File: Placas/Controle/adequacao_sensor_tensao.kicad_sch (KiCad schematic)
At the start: 6 parts, among them J5 Conn_01x02_Pin, U3 LV25-P

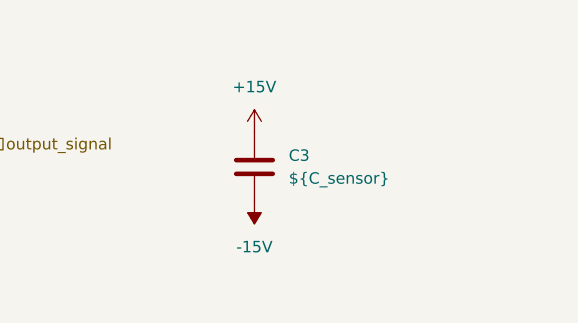
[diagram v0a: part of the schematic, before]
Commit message: Adição de circuitos opcionais para PWM
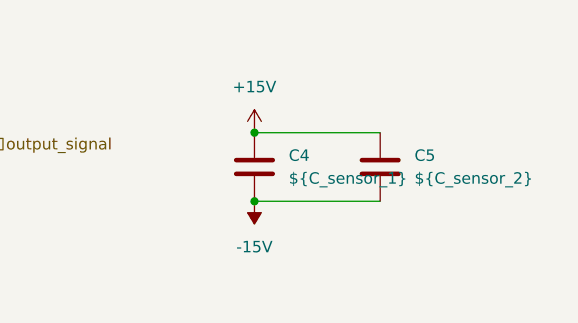
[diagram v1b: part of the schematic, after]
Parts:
- added C5: ${C_sensor_2}, Capacitor_THT:C_Disc_D8.0mm_W5.0mm_P7.50mm, symbol Device:C
- C4: renamed from C3; value ${C_sensor} -> ${C_sensor_1}
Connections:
- net +15V: now also C5.1
- net -15V: now also C5.2
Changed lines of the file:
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@@
+		(color 0 0 0 0)
+	)
+	(junction
+		(at 161.29 71.12)
+		(diameter 0)
+		(color 0 0 0 0)
+	)
+	(junction
+		(at 161.29 78.74)
+		(diameter 0)
 		(color 0 0 0 0)
 	)
@@
 	(wire
 		(pts
-			(xy 60.96 72.39) (xy 60.96 74.93)
+			(xy 161.29 78.74) (xy 175.26 78.74)
 		)
 		(stroke
@@
 	(wire
 		(pts
-			(xy 120.65 72.39) (xy 109.22 72.39)
+			(xy 60.96 72.39) (xy 60.96 74.93)
 		)
 		(stroke
@@
 	(wire
 		(pts
-			(xy 120.65 72.39) (xy 132.08 72.39)
+			(xy 120.65 72.39) (xy 109.22 72.39)
 		)
 		(stroke
@@
 	(wire
 		(pts
-			(xy 85.09 69.85) (xy 88.9 69.85)
+			(xy 120.65 72.39) (xy 132.08 72.39)
 		)
 		(stroke
@@
 	(wire
 		(pts
+			(xy 85.09 69.85) (xy 88.9 69.85)
+		)
+		(stroke
+			(width 0)
+			(type default)
+		)
+	)
+	(wire
+		(pts
 			(xy 74.93 69.85) (xy 77.47 69.85)
+		)
+		(stroke
+			(width 0)
+			(type default)
+		)
+	)
+	(wire
+		(pts
+			(xy 161.29 71.12) (xy 175.26 71.12)
 		)
 		(stroke
@@
 		(dnp no)
 		(fields_autoplaced yes)
-		(property "Reference" "#PWR18"
+		(property "Reference" "#PWR20"
 			(at 161.29 74.93 0)
 			(effects
@@
 			(project "board"
 				(path "/01568b53-f202-4f02-9c1a-9c10c7610b4b/64ed1ee1-6201-4cd1-840c-b46b599d55ab/9701d4b2-9f70-4dc2-8f65-3cb2cc418c7b"
-					(reference "#PWR18")
-					(unit 1)
-				)
-				(path "/01568b53-f202-4f02-9c1a-9c10c7610b4b/64ed1ee1-6201-4cd1-840c-b46b599d55ab/d6523acf-4a35-49b3-8df2-392463f7dfc0"
-					(reference "#PWR13")
+					(reference "#PWR20")
+					(unit 1)
+				)
+				(path "/01568b53-f202-4f02-9c1a-9c10c7610b4b/64ed1ee1-6201-4cd1-840c-b46b599d55ab/d6523acf-4a35-49b3-8df2-392463f7dfc0"
+					(reference "#PWR15")
 					(unit 1)
 				)
@@
 	)
 	(symbol
+		(lib_id "Device:C")
+		(at 175.26 74.93 0)
+		(unit 1)
+		(exclude_from_sim no)
+		(in_bom yes)
+		(on_board yes)
+		(dnp no)
+		(fields_autoplaced yes)
+		(property "Reference" "C5"
+			(at 179.07 73.6599 0)
+			(effects
+				(font
+					(size 1.27 1.27)
+				)
+				(justify left)
+			)
+		)
+		(property "Value" "${C_sensor_2}"
+			(at 179.07 76.1999 0)
+			(effects
+				(font
+					(size 1.27 1.27)
+				)
+				(justify left)
+			)
+		)
+		(property "Footprint" "Capacitor_THT:C_Disc_D8.0mm_W5.0mm_P7.50mm"
+			(at 176.2252 78.74 0)
+			(effects
+				(font
+					(size 1.27 1.27)
+				)
+				(hide yes)
+			)
+		)
+		(property "Datasheet" "~"
+			(at 175.26 74.93 0)
+			(effects
+				(font
+					(size 1.27 1.27)
+				)
+				(hide yes)
+			)
+		)
+		(property "Description" "Unpolarized capacitor"
+			(at 175.26 74.93 0)
+			(effects
+				(font
+					(size 1.27 1.27)
+				)
+				(hide yes)
+			)
+		)
+		(pin "1"
+		)
+		(pin "2"
+		)
+		(instances
+			(project "Controle"
+				(path "/01568b53-f202-4f02-9c1a-9c10c7610b4b/64ed1ee1-6201-4cd1-840c-b46b599d55ab/9701d4b2-9f70-4dc2-8f65-3cb2cc418c7b"
+					(reference "C5")
+					(unit 1)
+				)
+				(path "/01568b53-f202-4f02-9c1a-9c10c7610b4b/64ed1ee1-6201-4cd1-840c-b46b599d55ab/d6523acf-4a35-49b3-8df2-392463f7dfc0"
+					(reference "C3")
+					(unit 1)
+				)
+			)
+		)
+	)
+	(symbol
 		(lib_id "Sensor_Voltage:LV25-P")
 		(at 99.06 72.39 0)
@@
 		(dnp no)
 		(fields_autoplaced yes)
-		(property "Reference" "#PWR15"
+		(property "Reference" "#PWR17"
 			(at 99.06 68.58 0)
 			(effects
@@
 			(project "board"
 				(path "/01568b53-f202-4f02-9c1a-9c10c7610b4b/64ed1ee1-6201-4cd1-840c-b46b599d55ab/9701d4b2-9f70-4dc2-8f65-3cb2cc418c7b"
-					(reference "#PWR15")
-					(unit 1)
-				)
-				(path "/01568b53-f202-4f02-9c1a-9c10c7610b4b/64ed1ee1-6201-4cd1-840c-b46b599d55ab/d6523acf-4a35-49b3-8df2-392463f7dfc0"
-					(reference "#PWR10")
+					(reference "#PWR17")
+					(unit 1)
+				)
+				(path "/01568b53-f202-4f02-9c1a-9c10c7610b4b/64ed1ee1-6201-4cd1-840c-b46b599d55ab/d6523acf-4a35-49b3-8df2-392463f7dfc0"
+					(reference "#PWR12")
 					(unit 1)
 				)
@@
 		(dnp no)
 		(fields_autoplaced yes)
-		(property "Reference" "C3"
+		(property "Reference" "C4"
 			(at 165.1 73.6599 0)
 			(effects
@@
 			)
 		)
-		(property "Value" "${C_sensor}"
+		(property "Value" "${C_sensor_1}"
 			(at 165.1 76.1999 0)
 			(effects
@@
 			(project "board"
 				(path "/01568b53-f202-4f02-9c1a-9c10c7610b4b/64ed1ee1-6201-4cd1-840c-b46b599d55ab/9701d4b2-9f70-4dc2-8f65-3cb2cc418c7b"
-					(reference "C3")
+					(reference "C4")
 					(unit 1)
 				)
@@
 		(dnp no)
 		(fields_autoplaced yes)
-		(property "Reference" "#PWR16"
+		(property "Reference" "#PWR18"
 			(at 99.06 76.2 0)
 			(effects
@@
 			(project "board"
 				(path "/01568b53-f202-4f02-9c1a-9c10c7610b4b/64ed1ee1-6201-4cd1-840c-b46b599d55ab/9701d4b2-9f70-4dc2-8f65-3cb2cc418c7b"
-					(reference "#PWR16")
-					(unit 1)
-				)
-				(path "/01568b53-f202-4f02-9c1a-9c10c7610b4b/64ed1ee1-6201-4cd1-840c-b46b599d55ab/d6523acf-4a35-49b3-8df2-392463f7dfc0"
-					(reference "#PWR11")
+					(reference "#PWR18")
+					(unit 1)
+				)
+				(path "/01568b53-f202-4f02-9c1a-9c10c7610b4b/64ed1ee1-6201-4cd1-840c-b46b599d55ab/d6523acf-4a35-49b3-8df2-392463f7dfc0"
+					(reference "#PWR13")
 					(unit 1)
 				)
@@
 		(dnp no)
 		(fields_autoplaced yes)
-		(property "Reference" "#PWR17"
+		(property "Reference" "#PWR19"
 			(at 120.65 90.17 0)
 			(effects
@@
 			(project "board"
 				(path "/01568b53-f202-4f02-9c1a-9c10c7610b4b/64ed1ee1-6201-4cd1-840c-b46b599d55ab/9701d4b2-9f70-4dc2-8f65-3cb2cc418c7b"
-					(reference "#PWR17")
-					(unit 1)
-				)
-				(path "/01568b53-f202-4f02-9c1a-9c10c7610b4b/64ed1ee1-6201-4cd1-840c-b46b599d55ab/d6523acf-4a35-49b3-8df2-392463f7dfc0"
-					(reference "#PWR12")
+					(reference "#PWR19")
+					(unit 1)
+				)
+				(path "/01568b53-f202-4f02-9c1a-9c10c7610b4b/64ed1ee1-6201-4cd1-840c-b46b599d55ab/d6523acf-4a35-49b3-8df2-392463f7dfc0"
+					(reference "#PWR14")
 					(unit 1)
 				)
@@
 		(dnp no)
 		(fields_autoplaced yes)
-		(property "Reference" "#PWR19"
+		(property "Reference" "#PWR21"
 			(at 161.29 74.93 0)
 			(effects
@@
 			(project "board"
 				(path "/01568b53-f202-4f02-9c1a-9c10c7610b4b/64ed1ee1-6201-4cd1-840c-b46b599d55ab/9701d4b2-9f70-4dc2-8f65-3cb2cc418c7b"
-					(reference "#PWR19")
-					(unit 1)
-				)
-				(path "/01568b53-f202-4f02-9c1a-9c10c7610b4b/64ed1ee1-6201-4cd1-840c-b46b599d55ab/d6523acf-4a35-49b3-8df2-392463f7dfc0"
-					(reference "#PWR14")
-					(unit 1)
-				)
+					(reference "#PWR21")
+					(unit 1)
+				)
+				(path "/01568b53-f202-4f02-9c1a-9c10c7610b4b/64ed1ee1-6201-4cd1-840c-b46b599d55ab/d6523acf-4a35-49b3-8df2-392463f7dfc0"
+					(reference "#PWR16")
+					(unit 1)
+				)

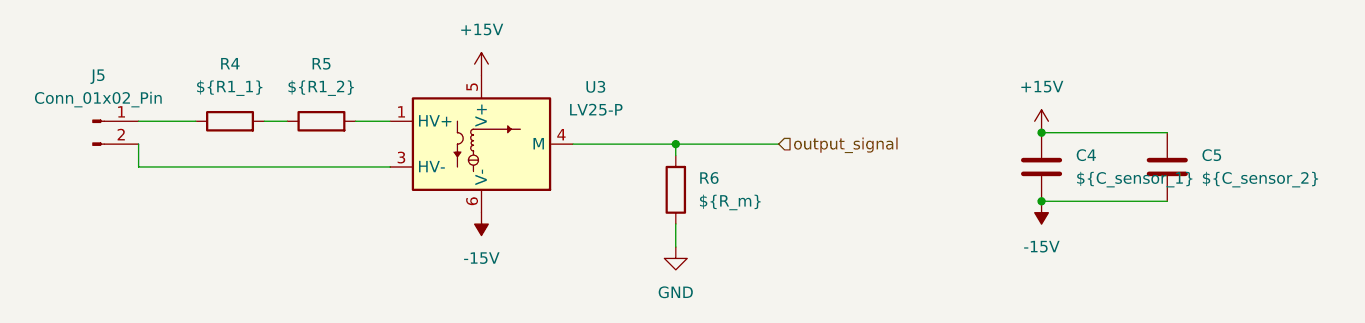
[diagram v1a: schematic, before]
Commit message: Modificações nas duas placas, adição de furos para montagem, melhora na posição dos micros e conectores para comunicação SPI
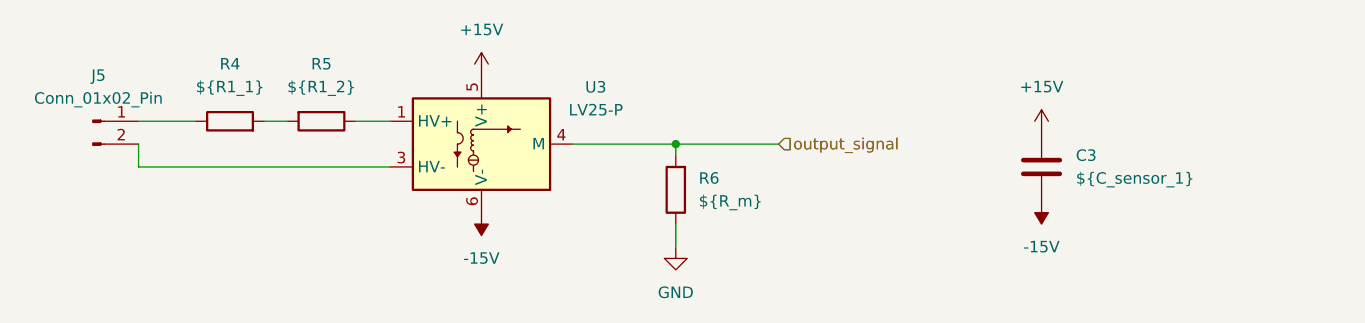
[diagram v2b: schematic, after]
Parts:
- removed C5: ${C_sensor_2}, Capacitor_THT:C_Disc_D8.0mm_W5.0mm_P7.50mm, symbol Device:C
- C3: renamed from C4; footprint Capacitor_THT:C_Disc_D8.0mm_W5.0mm_P7.50mm -> Capacitor_SMD:C_0805_2012Metric_Pad1.18x1.45mm_HandSolder
- R4: footprint Resistor_THT:R_Axial_DIN0207_L6.3mm_D2.5mm_P7.62mm_Horizontal -> Resistor_THT:R_Axial_DIN0614_L14.3mm_D5.7mm_P5.08mm_Vertical
- R5: footprint Resistor_THT:R_Axial_DIN0207_L6.3mm_D2.5mm_P7.62mm_Horizontal -> Resistor_THT:R_Axial_DIN0516_L15.5mm_D5.0mm_P5.08mm_Vertical
- R6: footprint Resistor_THT:R_Axial_DIN0207_L6.3mm_D2.5mm_P7.62mm_Horizontal -> Resistor_SMD:R_0805_2012Metric_Pad1.20x1.40mm_HandSolder
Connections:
- net at R4.2: now also R5.2; no longer R5.1
- net at U3.1 (HV+): now also R5.1; no longer R5.2
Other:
- moved on the sheet: R5
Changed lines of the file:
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@@
-		(color 0 0 0 0)
-	)
-	(junction
-		(at 161.29 71.12)
-		(diameter 0)
-		(color 0 0 0 0)
-	)
-	(junction
-		(at 161.29 78.74)
-		(diameter 0)
 		(color 0 0 0 0)
 	)
@@
 	(wire
 		(pts
-			(xy 161.29 78.74) (xy 175.26 78.74)
+			(xy 60.96 72.39) (xy 60.96 74.93)
 		)
 		(stroke
@@
 	(wire
 		(pts
-			(xy 60.96 72.39) (xy 60.96 74.93)
+			(xy 120.65 72.39) (xy 109.22 72.39)
 		)
 		(stroke
@@
 	(wire
 		(pts
-			(xy 120.65 72.39) (xy 109.22 72.39)
+			(xy 120.65 72.39) (xy 132.08 72.39)
 		)
 		(stroke
@@
 	(wire
 		(pts
-			(xy 120.65 72.39) (xy 132.08 72.39)
+			(xy 74.93 69.85) (xy 77.47 69.85)
 		)
 		(stroke
@@
 		(pts
 			(xy 85.09 69.85) (xy 88.9 69.85)
-		)
-		(stroke
-			(width 0)
-			(type default)
-		)
-	)
-	(wire
-		(pts
-			(xy 74.93 69.85) (xy 77.47 69.85)
-		)
-		(stroke
-			(width 0)
-			(type default)
-		)
-	)
-	(wire
-		(pts
-			(xy 161.29 71.12) (xy 175.26 71.12)
 		)
 		(stroke
@@
 			)
 		)
-		(property "Footprint" "Resistor_THT:R_Axial_DIN0207_L6.3mm_D2.5mm_P7.62mm_Horizontal"
+		(property "Footprint" "Resistor_THT:R_Axial_DIN0614_L14.3mm_D5.7mm_P5.08mm_Vertical"
 			(at 71.12 71.628 90)
 			(effects
@@
 		(dnp no)
 		(fields_autoplaced yes)
-		(property "Reference" "#PWR20"
+		(property "Reference" "#PWR26"
 			(at 161.29 74.93 0)
 			(effects
@@
 			(project "board"
 				(path "/01568b53-f202-4f02-9c1a-9c10c7610b4b/64ed1ee1-6201-4cd1-840c-b46b599d55ab/9701d4b2-9f70-4dc2-8f65-3cb2cc418c7b"
-					(reference "#PWR20")
-					(unit 1)
-				)
-				(path "/01568b53-f202-4f02-9c1a-9c10c7610b4b/64ed1ee1-6201-4cd1-840c-b46b599d55ab/d6523acf-4a35-49b3-8df2-392463f7dfc0"
-					(reference "#PWR15")
+					(reference "#PWR26")
+					(unit 1)
+				)
+				(path "/01568b53-f202-4f02-9c1a-9c10c7610b4b/64ed1ee1-6201-4cd1-840c-b46b599d55ab/d6523acf-4a35-49b3-8df2-392463f7dfc0"
+					(reference "#PWR21")
 					(unit 1)
 				)
@@
 	)
 	(symbol
-		(lib_id "Device:C")
-		(at 175.26 74.93 0)
-		(unit 1)
-		(exclude_from_sim no)
-		(in_bom yes)
-		(on_board yes)
-		(dnp no)
-		(fields_autoplaced yes)
-		(property "Reference" "C5"
-			(at 179.07 73.6599 0)
-			(effects
-				(font
-					(size 1.27 1.27)
-				)
-				(justify left)
-			)
-		)
-		(property "Value" "${C_sensor_2}"
-			(at 179.07 76.1999 0)
-			(effects
-				(font
-					(size 1.27 1.27)
-				)
-				(justify left)
-			)
-		)
-		(property "Footprint" "Capacitor_THT:C_Disc_D8.0mm_W5.0mm_P7.50mm"
-			(at 176.2252 78.74 0)
-			(effects
-				(font
-					(size 1.27 1.27)
-				)
-				(hide yes)
-			)
-		)
-		(property "Datasheet" "~"
-			(at 175.26 74.93 0)
-			(effects
-				(font
-					(size 1.27 1.27)
-				)
-				(hide yes)
-			)
-		)
-		(property "Description" "Unpolarized capacitor"
-			(at 175.26 74.93 0)
-			(effects
-				(font
-					(size 1.27 1.27)
-				)
-				(hide yes)
-			)
-		)
-		(pin "1"
-		)
-		(pin "2"
-		)
-		(instances
-			(project "Controle"
-				(path "/01568b53-f202-4f02-9c1a-9c10c7610b4b/64ed1ee1-6201-4cd1-840c-b46b599d55ab/9701d4b2-9f70-4dc2-8f65-3cb2cc418c7b"
-					(reference "C5")
-					(unit 1)
-				)
-				(path "/01568b53-f202-4f02-9c1a-9c10c7610b4b/64ed1ee1-6201-4cd1-840c-b46b599d55ab/d6523acf-4a35-49b3-8df2-392463f7dfc0"
-					(reference "C3")
-					(unit 1)
-				)
-			)
-		)
-	)
-	(symbol
 		(lib_id "Sensor_Voltage:LV25-P")
 		(at 99.06 72.39 0)
@@
 		(dnp no)
 		(fields_autoplaced yes)
-		(property "Reference" "#PWR17"
+		(property "Reference" "#PWR23"
 			(at 99.06 68.58 0)
 			(effects
@@
 			(project "board"
 				(path "/01568b53-f202-4f02-9c1a-9c10c7610b4b/64ed1ee1-6201-4cd1-840c-b46b599d55ab/9701d4b2-9f70-4dc2-8f65-3cb2cc418c7b"
-					(reference "#PWR17")
-					(unit 1)
-				)
-				(path "/01568b53-f202-4f02-9c1a-9c10c7610b4b/64ed1ee1-6201-4cd1-840c-b46b599d55ab/d6523acf-4a35-49b3-8df2-392463f7dfc0"
-					(reference "#PWR12")
+					(reference "#PWR23")
+					(unit 1)
+				)
+				(path "/01568b53-f202-4f02-9c1a-9c10c7610b4b/64ed1ee1-6201-4cd1-840c-b46b599d55ab/d6523acf-4a35-49b3-8df2-392463f7dfc0"
+					(reference "#PWR18")
 					(unit 1)
 				)
@@
 			)
 		)
-		(property "Footprint" "Resistor_THT:R_Axial_DIN0207_L6.3mm_D2.5mm_P7.62mm_Horizontal"
+		(property "Footprint" "Resistor_SMD:R_0805_2012Metric_Pad1.20x1.40mm_HandSolder"
 			(at 122.428 77.47 90)
 			(effects
@@
 		(dnp no)
 		(fields_autoplaced yes)
-		(property "Reference" "C4"
+		(property "Reference" "C3"
 			(at 165.1 73.6599 0)
 			(effects
@@
 			)
 		)
-		(property "Footprint" "Capacitor_THT:C_Disc_D8.0mm_W5.0mm_P7.50mm"
+		(property "Footprint" "Capacitor_SMD:C_0805_2012Metric_Pad1.18x1.45mm_HandSolder"
 			(at 162.2552 78.74 0)
 			(effects
@@
 			(project "board"
 				(path "/01568b53-f202-4f02-9c1a-9c10c7610b4b/64ed1ee1-6201-4cd1-840c-b46b599d55ab/9701d4b2-9f70-4dc2-8f65-3cb2cc418c7b"
-					(reference "C4")
+					(reference "C3")
 					(unit 1)
 				)
@@
 	(symbol
 		(lib_id "Device:R")
-		(at 81.28 69.85 90)
+		(at 81.28 69.85 270)
 		(unit 1)
 		(exclude_from_sim no)
@@
 			)
 		)
-		(property "Footprint" "Resistor_THT:R_Axial_DIN0207_L6.3mm_D2.5mm_P7.62mm_Horizontal"
-			(at 81.28 71.628 90)
+		(property "Footprint" "Resistor_THT:R_Axial_DIN0516_L15.5mm_D5.0mm_P5.08mm_Vertical"
+			(at 81.28 68.072 90)
 			(effects
 				(font
@@
 		(dnp no)
 		(fields_autoplaced yes)
-		(property "Reference" "#PWR18"
+		(property "Reference" "#PWR24"
 			(at 99.06 76.2 0)
 			(effects
@@
 			(project "board"
 				(path "/01568b53-f202-4f02-9c1a-9c10c7610b4b/64ed1ee1-6201-4cd1-840c-b46b599d55ab/9701d4b2-9f70-4dc2-8f65-3cb2cc418c7b"
-					(reference "#PWR18")
-					(unit 1)
-				)
-				(path "/01568b53-f202-4f02-9c1a-9c10c7610b4b/64ed1ee1-6201-4cd1-840c-b46b599d55ab/d6523acf-4a35-49b3-8df2-392463f7dfc0"
-					(reference "#PWR13")
+					(reference "#PWR24")
+					(unit 1)
+				)
+				(path "/01568b53-f202-4f02-9c1a-9c10c7610b4b/64ed1ee1-6201-4cd1-840c-b46b599d55ab/d6523acf-4a35-49b3-8df2-392463f7dfc0"
+					(reference "#PWR19")
 					(unit 1)
 				)
@@
 		(dnp no)
 		(fields_autoplaced yes)
-		(property "Reference" "#PWR19"
+		(property "Reference" "#PWR25"
 			(at 120.65 90.17 0)
 			(effects
@@
 			(project "board"
 				(path "/01568b53-f202-4f02-9c1a-9c10c7610b4b/64ed1ee1-6201-4cd1-840c-b46b599d55ab/9701d4b2-9f70-4dc2-8f65-3cb2cc418c7b"
-					(reference "#PWR19")
-					(unit 1)
-				)
-				(path "/01568b53-f202-4f02-9c1a-9c10c7610b4b/64ed1ee1-6201-4cd1-840c-b46b599d55ab/d6523acf-4a35-49b3-8df2-392463f7dfc0"
-					(reference "#PWR14")
+					(reference "#PWR25")
+					(unit 1)
+				)
+				(path "/01568b53-f202-4f02-9c1a-9c10c7610b4b/64ed1ee1-6201-4cd1-840c-b46b599d55ab/d6523acf-4a35-49b3-8df2-392463f7dfc0"
+					(reference "#PWR20")
 					(unit 1)
 				)
@@
 		(dnp no)
 		(fields_autoplaced yes)
-		(property "Reference" "#PWR21"
+		(property "Reference" "#PWR27"
 			(at 161.29 74.93 0)
 			(effects
@@
 			(project "board"
 				(path "/01568b53-f202-4f02-9c1a-9c10c7610b4b/64ed1ee1-6201-4cd1-840c-b46b599d55ab/9701d4b2-9f70-4dc2-8f65-3cb2cc418c7b"
-					(reference "#PWR21")
-					(unit 1)
-				)
-				(path "/01568b53-f202-4f02-9c1a-9c10c7610b4b/64ed1ee1-6201-4cd1-840c-b46b599d55ab/d6523acf-4a35-49b3-8df2-392463f7dfc0"
-					(reference "#PWR16")
-					(unit 1)
-				)
+					(reference "#PWR27")
+					(unit 1)
+				)
+				(path "/01568b53-f202-4f02-9c1a-9c10c7610b4b/64ed1ee1-6201-4cd1-840c-b46b599d55ab/d6523acf-4a35-49b3-8df2-392463f7dfc0"
+					(reference "#PWR22")
+					(unit 1)
+				)

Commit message: Criação dos arquivos em C para o firmware dos dois micros e script em python para salvar aquisição dos dados e envio de comandos
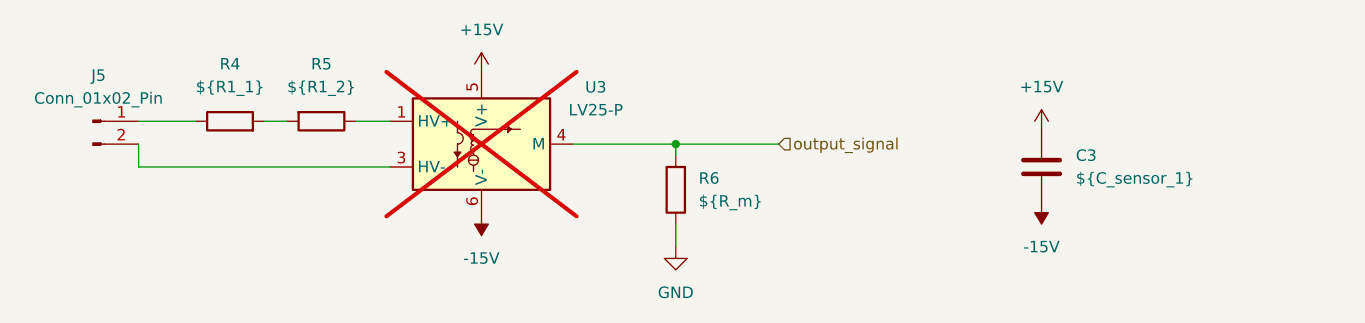
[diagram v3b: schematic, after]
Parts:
- U3: now not fitted
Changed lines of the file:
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@@
 		(in_bom yes)
 		(on_board yes)
-		(dnp no)
+		(dnp yes)
 		(fields_autoplaced yes)
 		(property "Reference" "U3"
